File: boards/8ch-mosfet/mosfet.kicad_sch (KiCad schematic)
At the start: 14 parts, among them J1 Screw_Terminal_01x02, Q1 IRFR7446, U5 ACS725xLCTR-20AU

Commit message: 8 channel mosfet driver also ready for proto
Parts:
- added R2: 1k, Resistor_SMD:R_0805_2012Metric_Pad1.20x1.40mm_HandSolder, symbol Device:R_Small_US
- F1: symbol gnarboard:ATC Fuse Bypass -> yarrboard:ATC Fuse Bypass
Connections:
- net ADC: now also R2.1; no longer U5.7 (VIOUT)
- new net: R2.2, U5.7 (VIOUT)
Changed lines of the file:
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@@
   (title_block
     (title "Yarrboard 8ch Mosfet Driver")
+    (rev "C")
     (company "https://github.com/hoeken/yarrboard")
+    (comment 1 "Open Source Hardware")
   )
   (junction (at 165.1 68.58) (diameter 0) (color 0 0 0 0)
@@
     (stroke (width 0) (type default))
   )
+  (wire (pts (xy 167.64 110.49) (xy 170.18 110.49))
+    (stroke (width 0) (type default))
+  )
   (wire (pts (xy 104.14 80.01) (xy 104.14 83.82))
     (stroke (width 0) (type default))
@@
     (stroke (width 0) (type default))
   )
-  (wire (pts (xy 160.02 110.49) (xy 170.18 110.49))
+  (wire (pts (xy 160.02 110.49) (xy 162.56 110.49))
     (stroke (width 0) (type default))
   )
@@
     )
   )
-  (symbol (lib_id "gnarboard:ATC Fuse Bypass") (at 165.1 68.58 0) (unit 1)
+  (symbol (lib_id "yarrboard:ATC Fuse Bypass") (at 165.1 68.58 0) (unit 1)
     (in_bom yes) (on_board yes) (dnp no)
     (property "Reference" "F1" (at 157.48 62.23 0)
@@
       (effects (font (size 1.27 1.27)) (justify left))
     )
-    (property "Footprint" "yarrboard:ATC Bypass Fuse" (at 162.052 64.77 90)
-      (effects (font (size 1.27 1.27)) hide)
-    )
-    (property "Datasheet" "~" (at 163.83 64.77 0)
+    (property "Footprint" "yarrboard:ATC Bypass Fuse" (at 163.322 63.5 90)
+      (effects (font (size 1.27 1.27)) hide)
+    )
+    (property "Datasheet" "~" (at 165.1 63.5 0)
       (effects (font (size 1.27 1.27)) hide)
     )
@@
         )
       )
+    )
+  )
+  (symbol (lib_id "Device:R_Small_US") (at 165.1 110.49 270) (unit 1)
+    (in_bom yes) (on_board yes) (dnp no) (fields_autoplaced)
+    (property "Reference" "R2" (at 165.1 104.14 90)
+      (effects (font (size 1.27 1.27)))
+    )
+    (property "Value" "1k" (at 165.1 106.68 90)
+      (effects (font (size 1.27 1.27)))
+    )
+    (property "Footprint" "Resistor_SMD:R_0805_2012Metric_Pad1.20x1.40mm_HandSolder" (at 165.1 110.49 0)
+      (effects (font (size 1.27 1.27)) hide)
+    )
+    (property "Datasheet" "~" (at 165.1 110.49 0)
+      (effects (font (size 1.27 1.27)) hide)
+    )
+    (property "LCSC" "C95781" (at 165.1 110.49 0)
+      (effects (font (size 1.27 1.27)) hide)
+    )
+    (pin "1")
+    (pin "2")
+    (instances
+      (project "8ch-mosfet"
+        (path "/c83c6236-96e9-46ad-9d7a-9e2efa4a7966"
+          (reference "R2") (unit 1)
+        )
+        (path "/c83c6236-96e9-46ad-9d7a-9e2efa4a7966/0eec6767-666b-42c0-ba36-2a83c9caeade"
+          (reference "R36") (unit 1)
+        )
+        (path "/c83c6236-96e9-46ad-9d7a-9e2efa4a7966/ccdb1c25-8d0f-4f30-ab70-bbc1ecf3f6f7"
+          (reference "R37") (unit 1)
+        )
+        (path "/c83c6236-96e9-46ad-9d7a-9e2efa4a7966/1e692482-a022-407a-8cb5-d9a3b23521a6"
+          (reference "R38") (unit 1)
+        )
+        (path "/c83c6236-96e9-46ad-9d7a-9e2efa4a7966/5952e660-2bb6-45cf-b9ea-f7a7c2d0954e"
+          (reference "R39") (unit 1)
+        )
+        (path "/c83c6236-96e9-46ad-9d7a-9e2efa4a7966/772d44f5-8758-48db-a140-72ed8e75e88c"
+          (reference "R40") (unit 1)
+        )
+        (path "/c83c6236-96e9-46ad-9d7a-9e2efa4a7966/424e7b24-5644-46f2-85bb-1e459a343705"
+          (reference "R41") (unit 1)
+        )
+        (path "/c83c6236-96e9-46ad-9d7a-9e2efa4a7966/4c1df725-56ca-4be4-8107-a39054acbca4"
+          (reference "R42") (unit 1)
+        )
+        (path "/c83c6236-96e9-46ad-9d7a-9e2efa4a7966/a8a81147-5613-4820-beb3-a7ca76d0db8e"
+          (reference "R43") (unit 1)
+        )
+      )

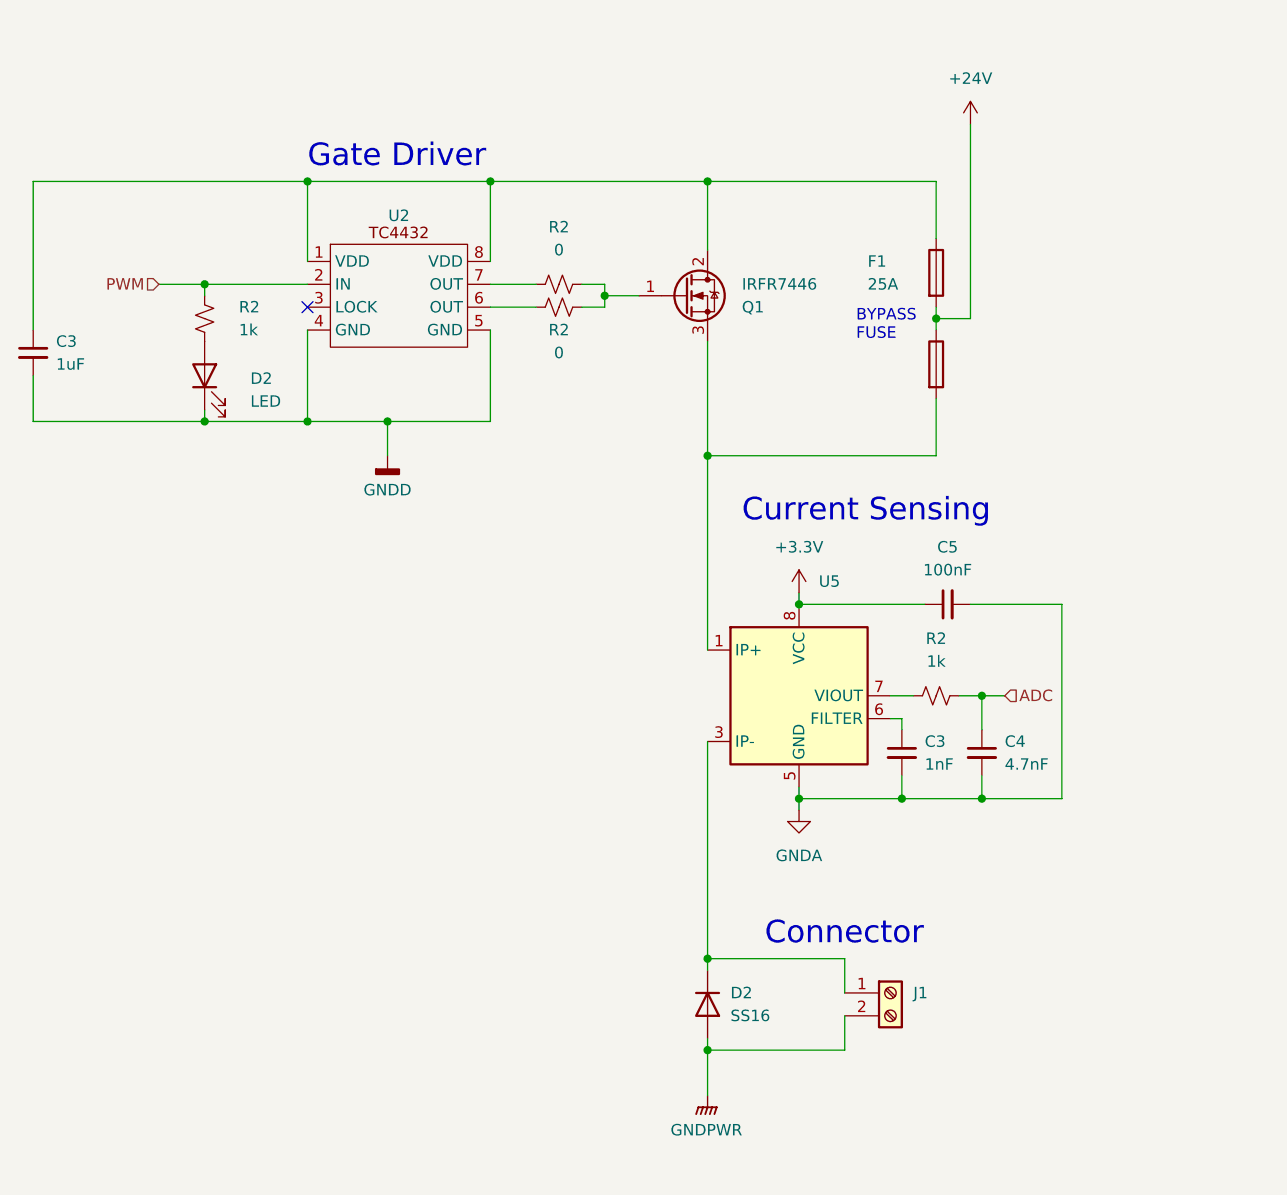
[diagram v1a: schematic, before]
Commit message: first commit of the 'totem pole' driver design
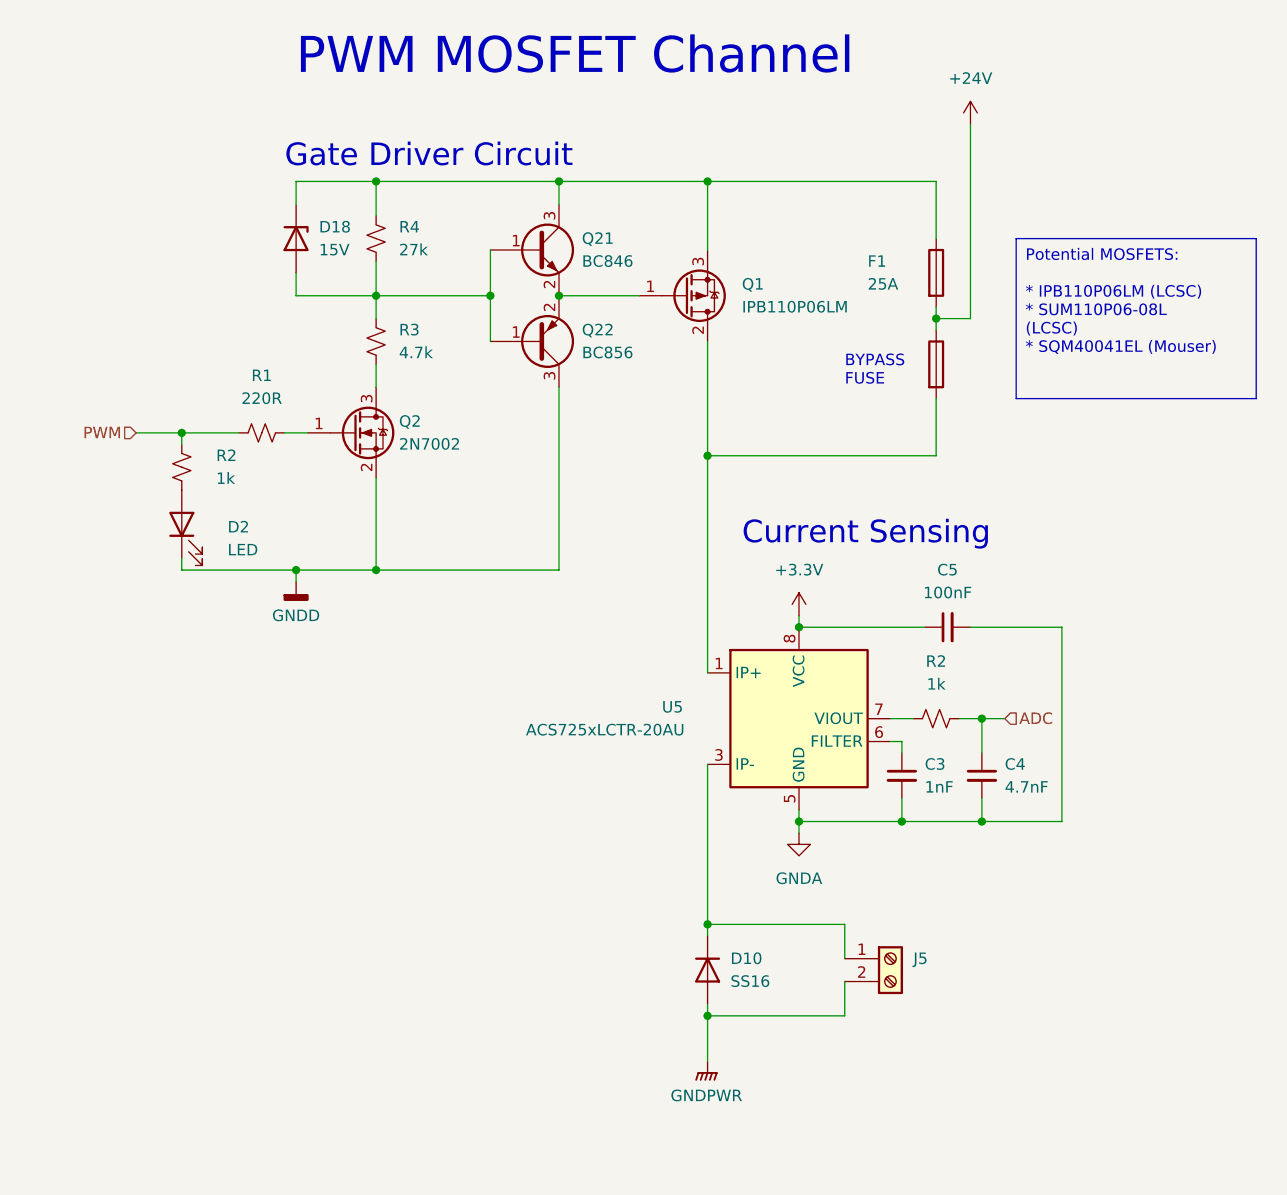
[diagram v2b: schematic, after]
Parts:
- removed C3: 1uF, Capacitor_SMD:C_0805_2012Metric_Pad1.18x1.45mm_HandSolder, symbol Device:C_Small
- removed R2: 1k, Resistor_SMD:R_0805_2012Metric_Pad1.20x1.40mm_HandSolder, symbol Device:R_Small_US
- removed R2 (x2): 0, Resistor_SMD:R_0805_2012Metric_Pad1.20x1.40mm_HandSolder, symbol Device:R_Small_US
- removed U2: ~, Package_SO:SOIC-8_3.9x4.9mm_P1.27mm, symbol yarrboard:TC4432
- added D18: 15V, Diode_SMD:D_SOD-323_HandSoldering, symbol Device:D_Zener
- added Q2: 2N7002, Package_TO_SOT_SMD:SOT-23, symbol Transistor_FET:2N7002
- added Q21: BC846, Package_TO_SOT_SMD:SOT-23, symbol Transistor_BJT:BC846
- added Q22: BC856, Package_TO_SOT_SMD:SOT-23, symbol Transistor_BJT:BC856
- added R1: 220R, Resistor_SMD:R_0805_2012Metric_Pad1.20x1.40mm_HandSolder, symbol Device:R_Small_US
- added R2: 1k, Resistor_SMD:R_0805_2012Metric_Pad1.20x1.40mm_HandSolder, symbol Device:R_Small_US
- added R3: 4.7k, Resistor_SMD:R_0805_2012Metric_Pad1.20x1.40mm_HandSolder, symbol Device:R_Small_US
- added R4: 27k, Resistor_SMD:R_0805_2012Metric_Pad1.20x1.40mm_HandSolder, symbol Device:R_Small_US
- F1: symbol yarrboard:ATC Fuse Bypass -> gnarboard:ATC Fuse Bypass
- Q1: value IRFR7446 -> IPB110P06LM; footprint Package_TO_SOT_SMD:TO-252-2 -> Package_TO_SOT_SMD:TO-263-2; symbol Transistor_FET:IRLZ44N -> Transistor_FET:IRF4905
- renumbered D2 to D10, J1 to J5
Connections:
- net ADC: now also R2.1
- net GNDD: now also Q2.2 (S), Q22.3 (C)
- net PWM: now also R1.1
- net at F1.1: now also Q1.3 (S), D18.1 (K), Q21.3 (C), R4.2; no longer Q1.2 (D)
- net at F1.3, U5.1 (IP+), U5.2 (IP+): now also Q1.2 (D); no longer Q1.3 (S)
- net at U5.7 (VIOUT): now also R2.2
- net at Q1.1 (G): now also Q21.2 (E), Q22.2 (E)
- new net: Q2.1 (G), R1.2
- new net: D18.2 (A), Q21.1 (B), Q22.1 (B), R3.2, R4.1
- new net: Q2.3 (D), R3.1
- no-connect marks 1 -> 0
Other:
- note added: "Gate Driver Circuit"
- note added: "PWM MOSFET Channel"
- note removed: "Connector"
- note removed: "Gate Driver"
- moved on the sheet: C3, C4, C5, D10, D2, J5, R2, U5

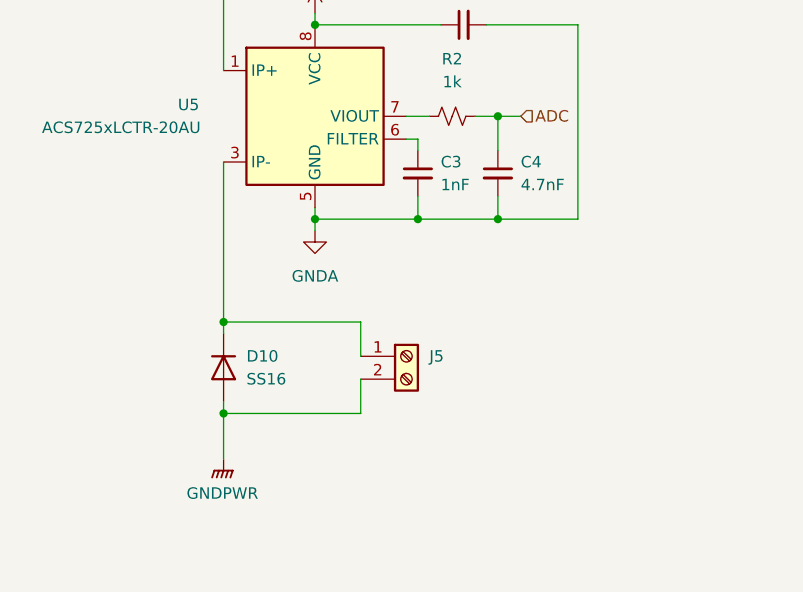
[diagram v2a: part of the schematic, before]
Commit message: oof, working from the wrong copy, had to redo some stuff
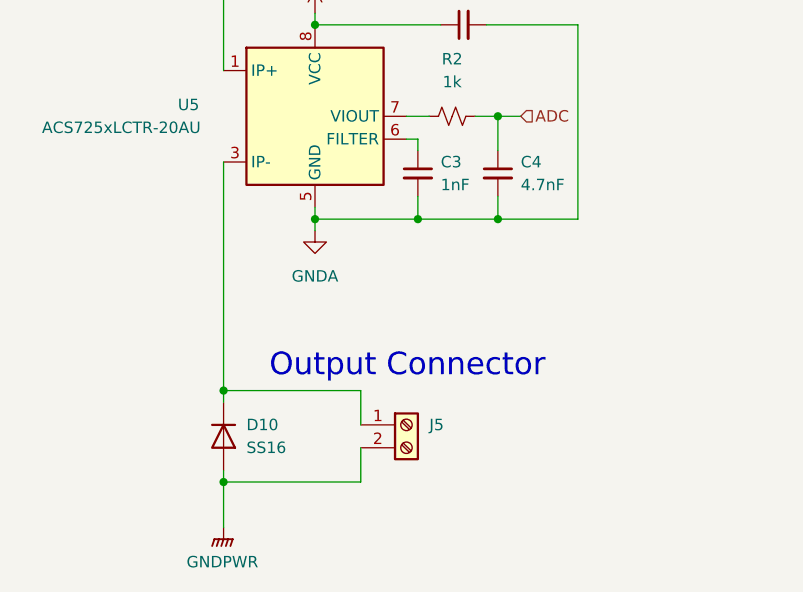
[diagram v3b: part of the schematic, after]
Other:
- note added: "Output Connector"
- moved on the sheet: D10, J5
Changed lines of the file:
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@@
   (title_block
     (title "Yarrboard 8ch Mosfet Driver")
+    (rev "C1")
     (company "https://github.com/hoeken/yarrboard")
   )
@@
   (junction (at 81.28 81.28) (diameter 0) (color 0 0 0 0)
   )
-  (junction (at 139.7 135.89) (diameter 0) (color 0 0 0 0)
+  (junction (at 139.7 143.51) (diameter 0) (color 0 0 0 0)
   )
   (junction (at 93.98 96.52) (diameter 0) (color 0 0 0 0)
@@
   (junction (at 123.19 66.04) (diameter 0) (color 0 0 0 0)
   )
-  (junction (at 139.7 146.05) (diameter 0) (color 0 0 0 0)
+  (junction (at 139.7 153.67) (diameter 0) (color 0 0 0 0)
   )
   (junction (at 102.87 96.52) (diameter 0) (color 0 0 0 0)
@@
     (stroke (width 0) (type default))
   )
-  (wire (pts (xy 139.7 146.05) (xy 139.7 151.13))
+  (wire (pts (xy 139.7 153.67) (xy 139.7 158.75))
     (stroke (width 0) (type default))
   )
@@
     (stroke (width 0) (type default))
   )
-  (wire (pts (xy 139.7 135.89) (xy 154.94 135.89))
-    (stroke (width 0) (type default))
-  )
-  (wire (pts (xy 139.7 146.05) (xy 154.94 146.05))
+  (wire (pts (xy 139.7 143.51) (xy 154.94 143.51))
+    (stroke (width 0) (type default))
+  )
+  (wire (pts (xy 139.7 153.67) (xy 154.94 153.67))
     (stroke (width 0) (type default))
   )
@@
     (stroke (width 0) (type default))
   )
-  (wire (pts (xy 154.94 146.05) (xy 154.94 142.24))
+  (wire (pts (xy 154.94 153.67) (xy 154.94 149.86))
     (stroke (width 0) (type default))
   )
@@
     (stroke (width 0) (type default))
   )
-  (wire (pts (xy 139.7 144.78) (xy 139.7 146.05))
+  (wire (pts (xy 139.7 152.4) (xy 139.7 153.67))
     (stroke (width 0) (type default))
   )
@@
     (stroke (width 0) (type default))
   )
-  (wire (pts (xy 139.7 118.11) (xy 139.7 135.89))
+  (wire (pts (xy 139.7 118.11) (xy 139.7 143.51))
     (stroke (width 0) (type default))
   )
@@
     (stroke (width 0) (type default))
   )
-  (wire (pts (xy 139.7 137.16) (xy 139.7 135.89))
+  (wire (pts (xy 139.7 144.78) (xy 139.7 143.51))
     (stroke (width 0) (type default))
   )
@@
     (stroke (width 0) (type default))
   )
-  (wire (pts (xy 154.94 135.89) (xy 154.94 139.7))
+  (wire (pts (xy 154.94 143.51) (xy 154.94 147.32))
     (stroke (width 0) (type default))
   )
@@
     (effects (font (size 1.27 1.27)) (justify left top))
   )
+  (text "Output Connector" (at 144.78 142.24 0)
+    (effects (font (size 2.5 2.5)) (justify left bottom))
+  )
   (text "Current Sensing" (at 143.51 93.98 0)
     (effects (font (size 2.5 2.5)) (justify left bottom))
@@
     )
   )
-  (symbol (lib_id "Diode:MRA4004T3G") (at 139.7 140.97 270) (unit 1)
-    (in_bom yes) (on_board yes) (dnp no) (fields_autoplaced)
-    (property "Reference" "D10" (at 142.24 139.7 90)
-      (effects (font (size 1.27 1.27)) (justify left))
-    )
-    (property "Value" "SS16" (at 142.24 142.24 90)
-      (effects (font (size 1.27 1.27)) (justify left))
-    )
-    (property "Footprint" "Diode_SMD:D_SMA" (at 135.255 140.97 0)
-      (effects (font (size 1.27 1.27)) hide)
-    )
-    (property "Datasheet" "" (at 139.7 140.97 0)
-      (effects (font (size 1.27 1.27)) hide)
-    )
-    (property "Sim.Device" "D" (at 139.7 140.97 0)
-      (effects (font (size 1.27 1.27)) hide)
-    )
-    (property "Sim.Pins" "1=K 2=A" (at 139.7 140.97 0)
-      (effects (font (size 1.27 1.27)) hide)
-    )
-    (property "Mouser" "625-SS16-E3 " (at 139.7 140.97 0)
+  (symbol (lib_id "Diode:MRA4004T3G") (at 139.7 148.59 270) (unit 1)
+    (in_bom yes) (on_board yes) (dnp no) (fields_autoplaced)
+    (property "Reference" "D10" (at 142.24 147.32 90)
+      (effects (font (size 1.27 1.27)) (justify left))
+    )
+    (property "Value" "SS16" (at 142.24 149.86 90)
+      (effects (font (size 1.27 1.27)) (justify left))
+    )
+    (property "Footprint" "Diode_SMD:D_SMA" (at 135.255 148.59 0)
+      (effects (font (size 1.27 1.27)) hide)
+    )
+    (property "Datasheet" "" (at 139.7 148.59 0)
+      (effects (font (size 1.27 1.27)) hide)
+    )
+    (property "Sim.Device" "D" (at 139.7 148.59 0)
+      (effects (font (size 1.27 1.27)) hide)
+    )
+    (property "Sim.Pins" "1=K 2=A" (at 139.7 148.59 0)
+      (effects (font (size 1.27 1.27)) hide)
+    )
+    (property "Mouser" "625-SS16-E3 " (at 139.7 148.59 0)
       (effects (font (size 1.27 1.27)) hide)
     )
@@
     )
   )
-  (symbol (lib_id "Connector:Screw_Terminal_01x02") (at 160.02 139.7 0) (unit 1)
-    (in_bom yes) (on_board yes) (dnp no) (fields_autoplaced)
-    (property "Reference" "J5" (at 162.56 139.7 0)
-      (effects (font (size 1.27 1.27)) (justify left))
-    )
-    (property "Value" "Screw_Terminal_01x02" (at 162.56 142.24 0)
+  (symbol (lib_id "Connector:Screw_Terminal_01x02") (at 160.02 147.32 0) (unit 1)
+    (in_bom yes) (on_board yes) (dnp no) (fields_autoplaced)
+    (property "Reference" "J5" (at 162.56 147.32 0)
+      (effects (font (size 1.27 1.27)) (justify left))
+    )
+    (property "Value" "Screw_Terminal_01x02" (at 162.56 149.86 0)
       (effects (font (size 1.27 1.27)) (justify left) hide)
     )
-    (property "Footprint" "yarrboard:Molex 1x02 .375" (at 160.02 139.7 0)
-      (effects (font (size 1.27 1.27)) hide)
-    )
-    (property "Datasheet" "~" (at 160.02 139.7 0)
-      (effects (font (size 1.27 1.27)) hide)
-    )
-    (property "Mouser" " 538-38720-7516" (at 160.02 139.7 0)
-      (effects (font (size 1.27 1.27)) hide)
-    )
-    (property "JCLC" "JL45C-09516B01" (at 160.02 139.7 0)
+    (property "Footprint" "yarrboard:Molex 1x02 .375" (at 160.02 147.32 0)
+      (effects (font (size 1.27 1.27)) hide)
+    )
+    (property "Datasheet" "~" (at 160.02 147.32 0)
+      (effects (font (size 1.27 1.27)) hide)
+    )
+    (property "Mouser" " 538-38720-7516" (at 160.02 147.32 0)
+      (effects (font (size 1.27 1.27)) hide)
+    )
+    (property "JCLC" "JL45C-09516B01" (at 160.02 147.32 0)
       (effects (font (size 1.27 1.27)) hide)
     )
@@
     )
   )
-  (symbol (lib_id "power:GNDPWR") (at 139.7 151.13 0) (unit 1)
-    (in_bom yes) (on_board yes) (dnp no) (fields_autoplaced)
-    (property "Reference" "#PWR013" (at 139.7 156.21 0)
-      (effects (font (size 1.27 1.27)) hide)
-    )
-    (property "Value" "GNDPWR" (at 139.573 154.94 0)
+  (symbol (lib_id "power:GNDPWR") (at 139.7 158.75 0) (unit 1)
+    (in_bom yes) (on_board yes) (dnp no) (fields_autoplaced)
+    (property "Reference" "#PWR013" (at 139.7 163.83 0)
+      (effects (font (size 1.27 1.27)) hide)
+    )
+    (property "Value" "GNDPWR" (at 139.573 162.56 0)
       (effects (font (size 1.27 1.27)))
     )
-    (property "Footprint" "" (at 139.7 152.4 0)
-      (effects (font (size 1.27 1.27)) hide)
-    )
-    (property "Datasheet" "" (at 139.7 152.4 0)
-      (effects (font (size 1.27 1.27)) hide)
-    )
+    (property "Footprint" "" (at 139.7 160.02 0)
+      (effects (font (size 1.27 1.27)) hide)
+    )
+    (property "Datasheet" "" (at 139.7 160.02 0)
+      (effects (font (size 1.27 1.27)) hide)
+    )

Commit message: changed p/n
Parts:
- Q2: Mouser 771-BC817-25-T/R -> (none)
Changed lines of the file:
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@@
       (effects (font (size 1.27 1.27)) (justify left) hide)
-    )
-    (property "Mouser" "771-BC817-25-T/R" (at 100.33 81.28 0)
-      (effects (font (size 1.27 1.27)) hide)
     )
     (pin "1")
